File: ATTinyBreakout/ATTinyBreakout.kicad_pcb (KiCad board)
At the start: 2 copper layers, 55.9 x 34.3 mm, 15 parts, among them J1 Conn_01x05, J2 949, J3 MiniFitPower, J4 ICSP, U1 IRFZ44N, U2 ATTINY85-20PU

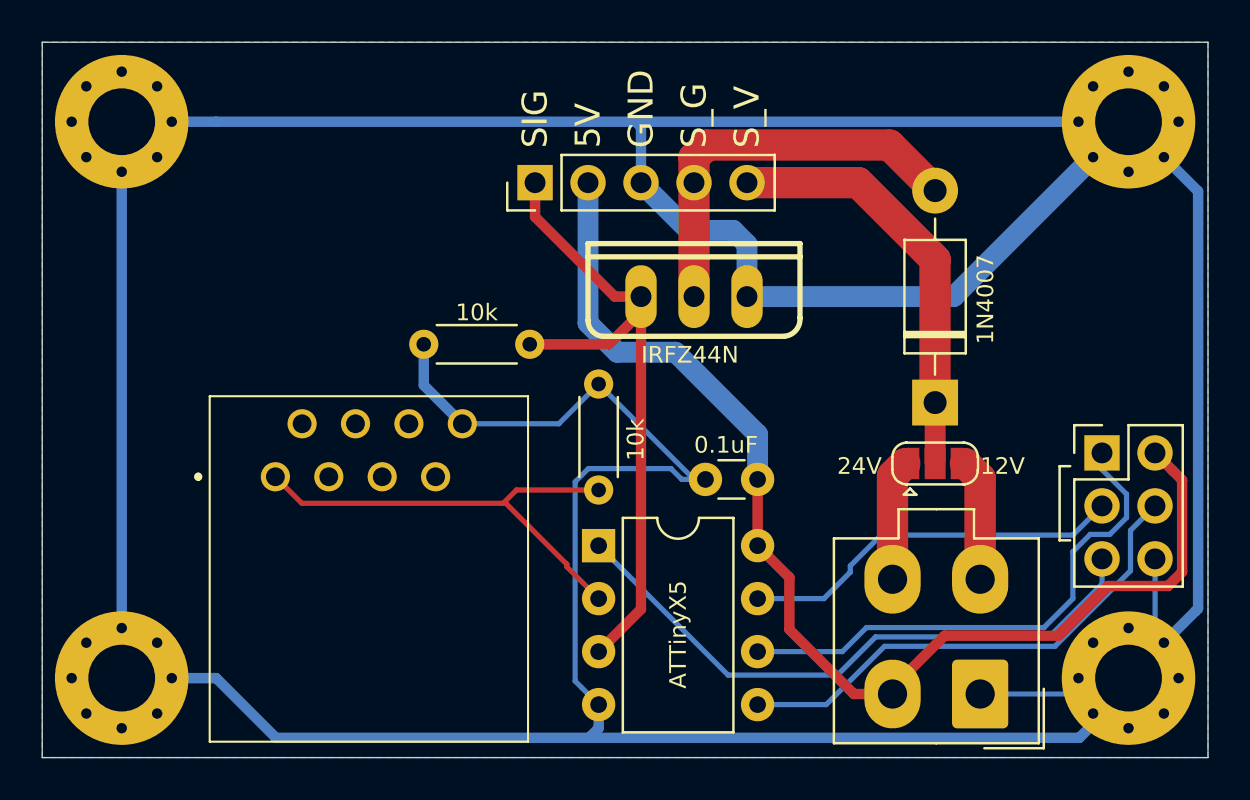
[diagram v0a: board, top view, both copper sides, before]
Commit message: Add adjust trimpot to attiny
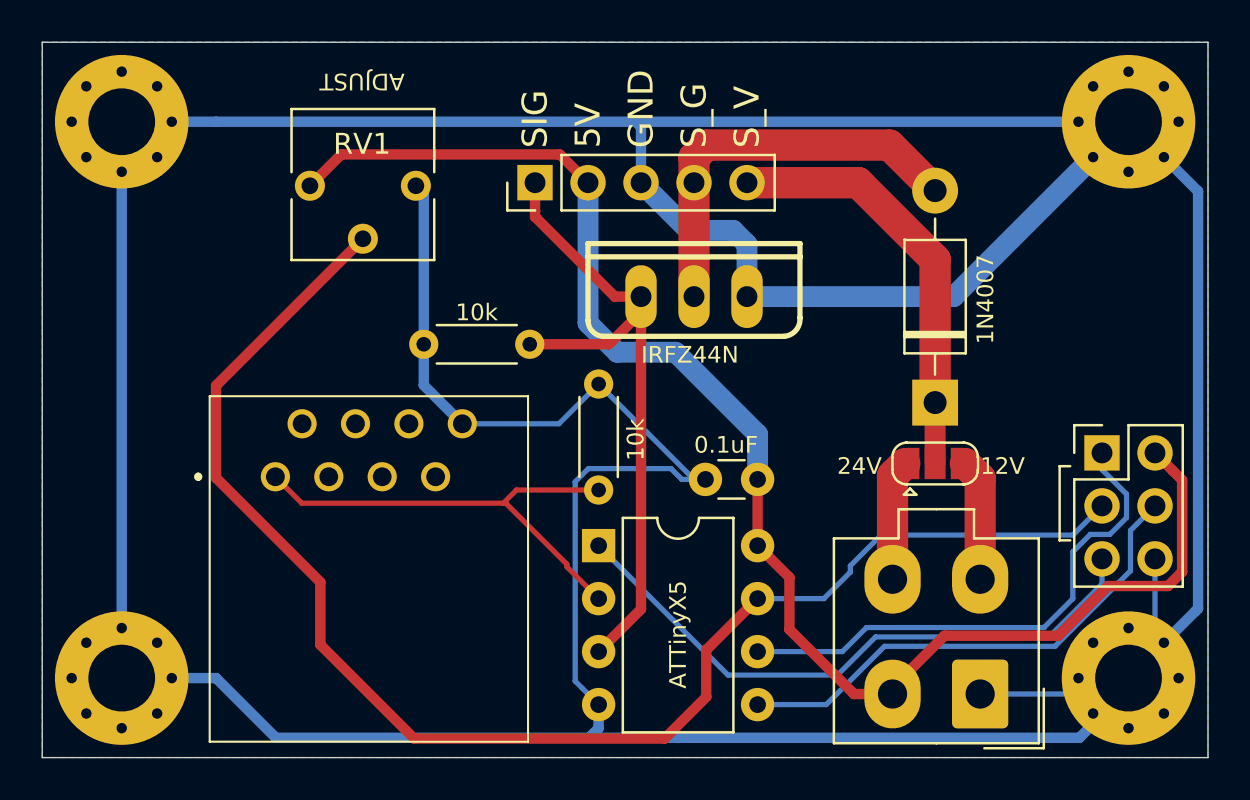
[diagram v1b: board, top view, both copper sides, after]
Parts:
- added RV1: TrimPot, Potentiometer_THT:Potentiometer_Vishay_T73YP_Vertical, F.Cu at (103.0, 78.0)
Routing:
- net SCK: track 18.5 -> 69.9 mm
- net 5V: track 56.0 -> 70.5 mm
- net GND: track 241.1 -> 248.9 mm
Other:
- board text added: "ADJUST"
